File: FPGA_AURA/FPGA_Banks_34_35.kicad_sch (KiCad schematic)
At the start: 15 parts, among them U1 XC7A35T-2FTG256C

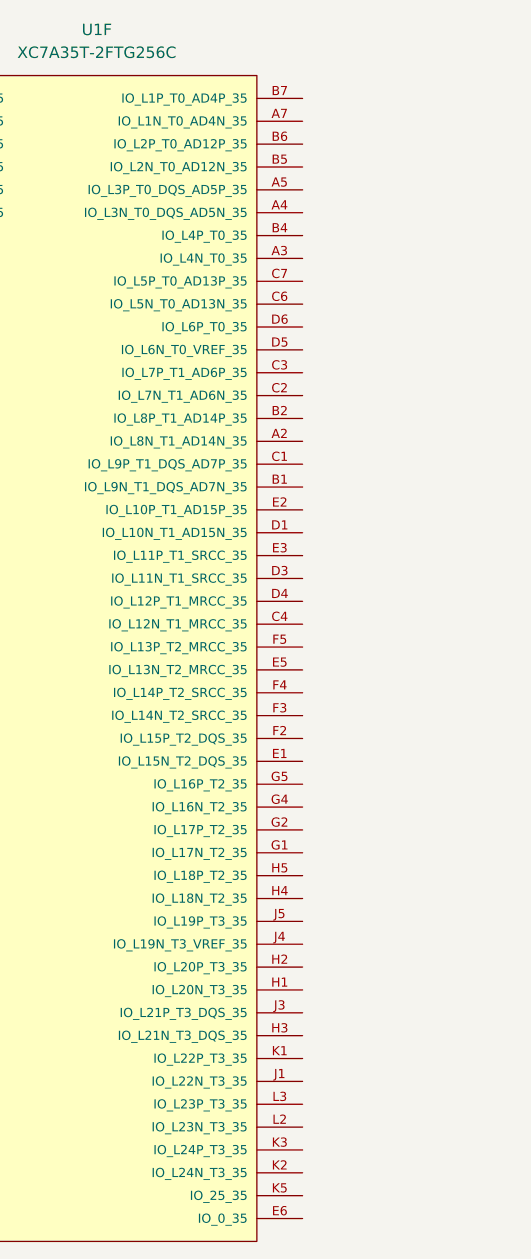
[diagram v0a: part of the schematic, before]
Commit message: Started pinout after successful Vivado bitstream generation.
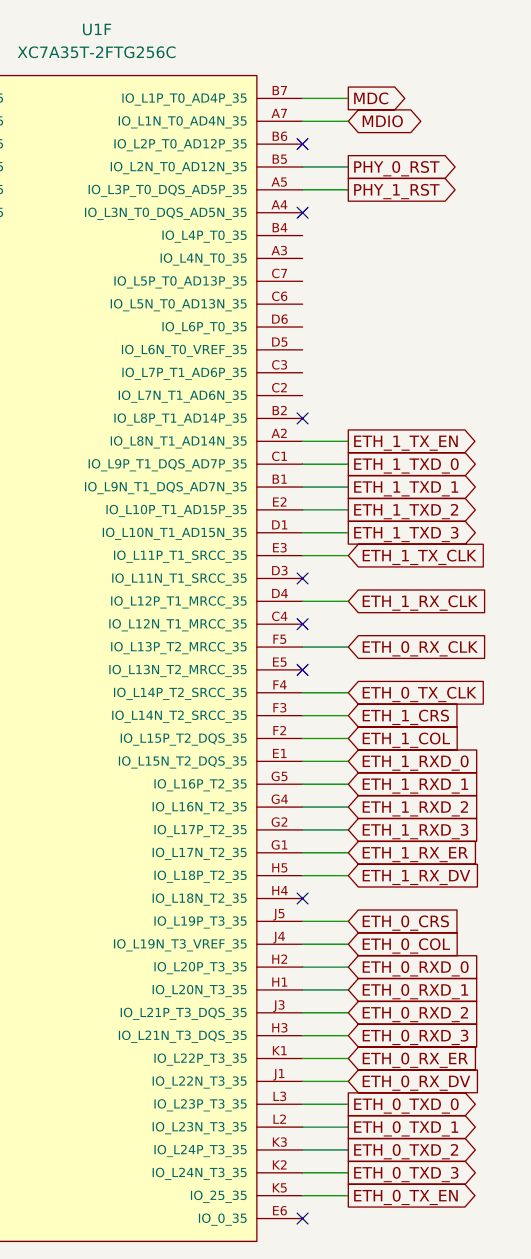
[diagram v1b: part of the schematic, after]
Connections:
- net ETH_1_TX_EN: now reaches U1.A2 (IO_L8N_T1_AD14N_35)
- net PHY_1_RST: now reaches U1.A5 (IO_L3P_T0_DQS_AD5P_35)
- net MDIO: now reaches U1.A7 (IO_L1N_T0_AD4N_35)
- net ETH_1_TXD_1: now reaches U1.B1 (IO_L9N_T1_DQS_AD7N_35)
- net PHY_0_RST: now reaches U1.B5 (IO_L2N_T0_AD12N_35)
- net MDC: now reaches U1.B7 (IO_L1P_T0_AD4P_35)
- net ETH_1_TXD_0: now reaches U1.C1 (IO_L9P_T1_DQS_AD7P_35)
- net ETH_1_TXD_3: now reaches U1.D1 (IO_L10N_T1_AD15N_35)
- net ETH_1_RX_CLK: now reaches U1.D4 (IO_L12P_T1_MRCC_35)
- net ETH_1_RXD_0: now reaches U1.E1 (IO_L15N_T2_DQS_35)
- net ETH_1_TXD_2: now reaches U1.E2 (IO_L10P_T1_AD15P_35)
- net ETH_1_TX_CLK: now reaches U1.E3 (IO_L11P_T1_SRCC_35)
- net ETH_1_COL: now reaches U1.F2 (IO_L15P_T2_DQS_35)
- net ETH_1_CRS: now reaches U1.F3 (IO_L14N_T2_SRCC_35)
- net ETH_0_TX_CLK: now reaches U1.F4 (IO_L14P_T2_SRCC_35)
- net ETH_0_RX_CLK: now reaches U1.F5 (IO_L13P_T2_MRCC_35)
- net ETH_1_RX_ER: now reaches U1.G1 (IO_L17N_T2_35)
- net ETH_1_RXD_3: now reaches U1.G2 (IO_L17P_T2_35)
- net ETH_1_RXD_2: now reaches U1.G4 (IO_L16N_T2_35)
- net ETH_1_RXD_1: now reaches U1.G5 (IO_L16P_T2_35)
- net ETH_0_RXD_1: now reaches U1.H1 (IO_L20N_T3_35)
- net ETH_0_RXD_0: now reaches U1.H2 (IO_L20P_T3_35)
- net ETH_0_RXD_3: now reaches U1.H3 (IO_L21N_T3_DQS_35)
- net ETH_1_RX_DV: now reaches U1.H5 (IO_L18P_T2_35)
- net ETH_0_RX_DV: now reaches U1.J1 (IO_L22N_T3_35)
- net ETH_0_RXD_2: now reaches U1.J3 (IO_L21P_T3_DQS_35)
- net ETH_0_COL: now reaches U1.J4 (IO_L19N_T3_VREF_35)
- net ETH_0_CRS: now reaches U1.J5 (IO_L19P_T3_35)
- net ETH_0_RX_ER: now reaches U1.K1 (IO_L22P_T3_35)
- net ETH_0_TXD_3: now reaches U1.K2 (IO_L24N_T3_35)
- net ETH_0_TXD_2: now reaches U1.K3 (IO_L24P_T3_35)
- net ETH_0_TX_EN: now reaches U1.K5 (IO_25_35)
- net ETH_0_TXD_1: now reaches U1.L2 (IO_L23N_T3_35)
- net ETH_0_TXD_0: now reaches U1.L3 (IO_L23P_T3_35)
- no-connect marks 0 -> 8

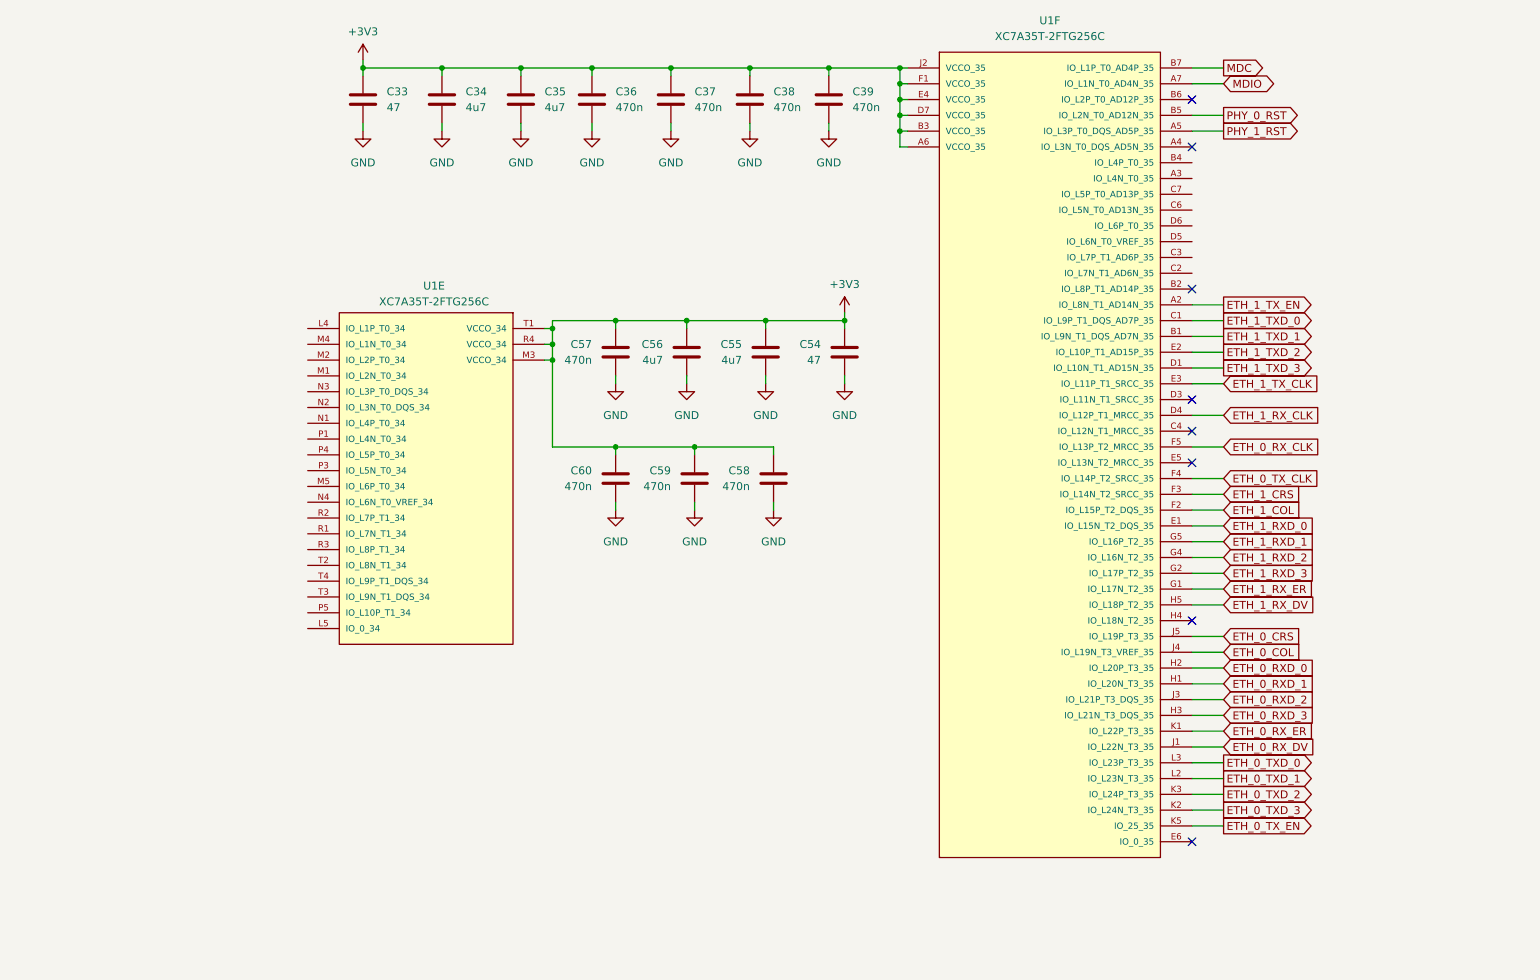
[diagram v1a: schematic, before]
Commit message: Connector pinnout defined loosly. Next is schematic clean-up followed by routing.
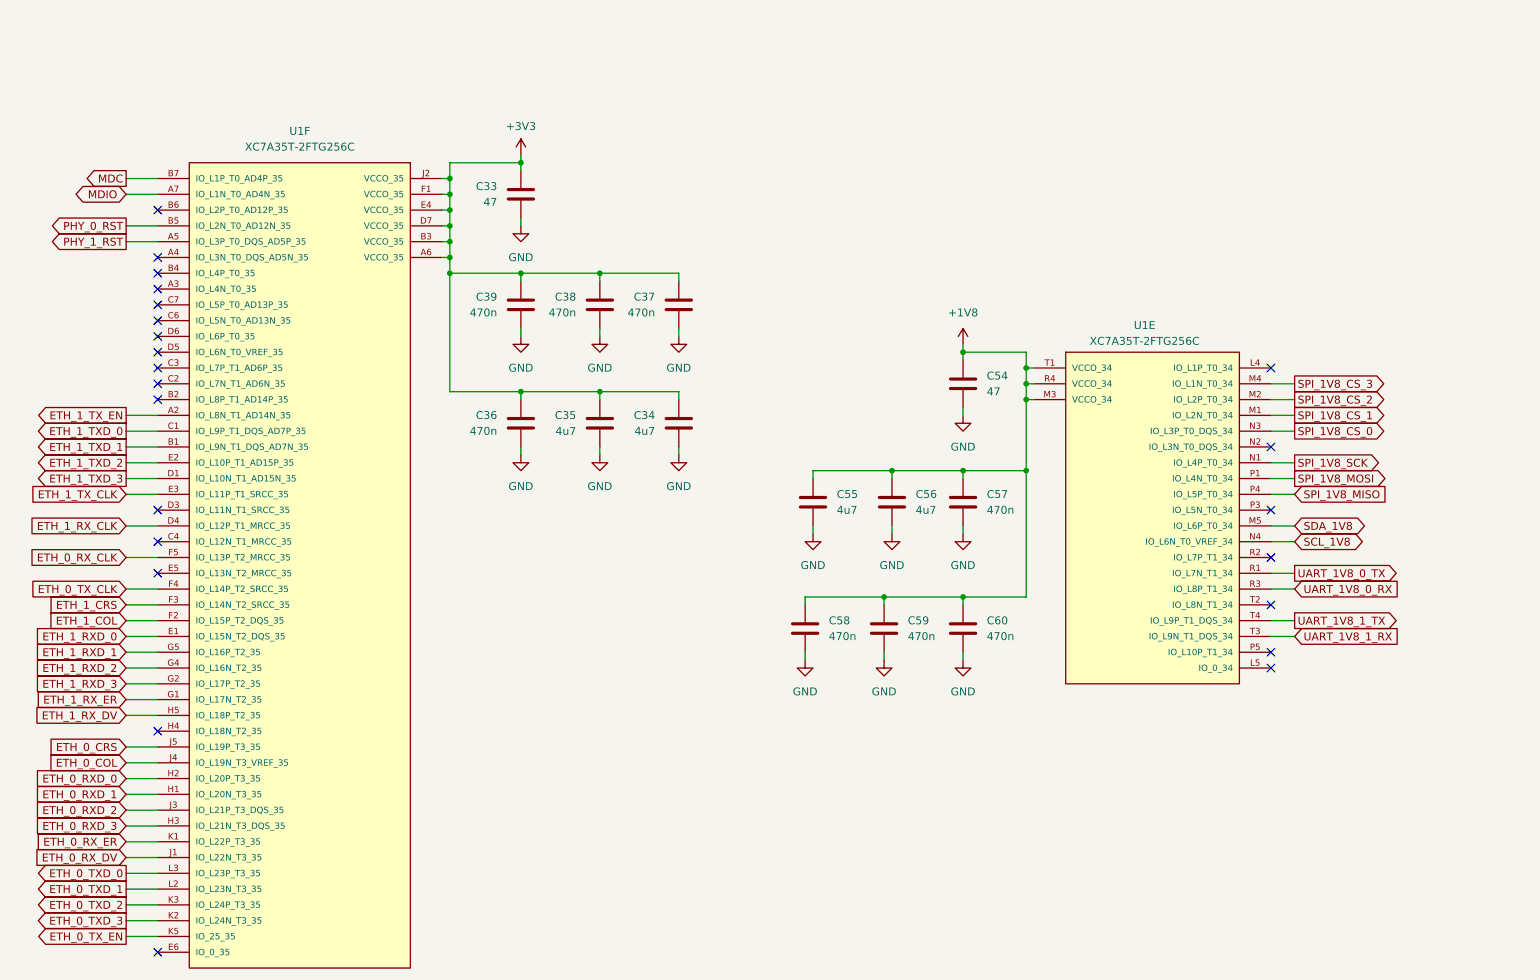
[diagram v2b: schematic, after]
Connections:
- net +3V3: no longer C54.1, C55.1, C56.1, C57.1, C58.1, C59.1, C60.1, U1.M3 (VCCO_34), U1.R4 (VCCO_34), U1.T1 (VCCO_34)
- net SPI_1V8_CS_1: now reaches U1.M1 (IO_L2N_T0_34)
- net SPI_1V8_CS_2: now reaches U1.M2 (IO_L2P_T0_34)
- net SPI_1V8_CS_3: now reaches U1.M4 (IO_L1N_T0_34)
- net SDA_1V8: now reaches U1.M5 (IO_L6P_T0_34)
- net SPI_1V8_SCK: now reaches U1.N1 (IO_L4P_T0_34)
- net SPI_1V8_CS_0: now reaches U1.N3 (IO_L3P_T0_DQS_34)
- net SCL_1V8: now reaches U1.N4 (IO_L6N_T0_VREF_34)
- net SPI_1V8_MOSI: now reaches U1.P1 (IO_L4N_T0_34)
- net SPI_1V8_MISO: now reaches U1.P4 (IO_L5P_T0_34)
- net UART_1V8_0_TX: now reaches U1.R1 (IO_L7N_T1_34)
- net UART_1V8_0_RX: now reaches U1.R3 (IO_L8P_T1_34)
- net UART_1V8_1_RX: now reaches U1.T3 (IO_L9N_T1_DQS_34)
- net UART_1V8_1_TX: now reaches U1.T4 (IO_L9P_T1_DQS_34)
- new net +1V8: C54.1, C55.1, C56.1, C57.1, C58.1, C59.1, C60.1, U1.M3 (VCCO_34), U1.R4 (VCCO_34), U1.T1 (VCCO_34)
- no-connect marks 8 -> 23
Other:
- moved on the sheet: C33, C34, C35, C36, C37, C38, C39, C54, C55, C56, C57, C58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

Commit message: Finished schematic to start routing again, and started MII fanout from connector.
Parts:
- C600: renamed from C33; value 47 -> 47u
- C607: renamed from C54; value 47 -> 47u
- renumbered C39 to C601, C38 to C602, C37 to C603, C36 to C604, C35 to C605, C34 to C606, C57 to C608, C56 to C609, C55 to C610, C60 to C611, C59 to C612, C58 to C613
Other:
- company: (none) -> Alexander Armitage
- title: (none) -> XC7A35T Banks 34, 35
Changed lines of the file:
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@@
 	(generator_version "10.0")
 	(paper "A4")
+	(title_block
+		(title "XC7A35T Banks 34, 35")
+		(company "Alexander Armitage")
+	)
 	(junction
 		(at 196.85 85.09)
@@
 		(dnp no)
 		(fields_autoplaced yes)
-		(property "Reference" "C39"
+		(property "Reference" "C601"
 			(at 111.76 68.5799 0)
 			(show_name no)
@@
 			(project "FPGA_AURA"
 				(path "/3d83cb23-9528-4d06-8969-599520e9eb23/2d3446c8-405c-4eaf-9ac6-0e0b69b3b124"
-					(reference "C39")
+					(reference "C601")
 					(unit 1)
 				)
@@
 		(dnp no)
 		(fields_autoplaced yes)
-		(property "Reference" "C58"
+		(property "Reference" "C613"
 			(at 165.1 120.6499 0)
 			(show_name no)
@@
 			(project "FPGA_AURA"
 				(path "/3d83cb23-9528-4d06-8969-599520e9eb23/2d3446c8-405c-4eaf-9ac6-0e0b69b3b124"
-					(reference "C58")
+					(reference "C613")
 					(unit 1)
 				)
@@
 		(lib_id "Device:C")
 		(at 115.57 88.9 0)
-		(mirror y)
 		(unit 1)
 		(body_style 1)
@@
 		(in_pos_files yes)
 		(dnp no)
-		(fields_autoplaced yes)
-		(property "Reference" "C36"
+		(property "Reference" "C604"
 			(at 111.76 87.6299 0)
 			(show_name no)
@@
 					(size 1.27 1.27)
 				)
-				(justify left)
+				(justify right)
 			)
 		)
@@
 					(size 1.27 1.27)
 				)
-				(justify left)
+				(justify right)
 			)
 		)
 		(property "Footprint" "Capacitor_SMD:C_0402_1005Metric"
-			(at 114.6048 92.71 0)
+			(at 116.5352 92.71 0)
 			(hide yes)
 			(show_name no)
@@
 			(project "FPGA_AURA"
 				(path "/3d83cb23-9528-4d06-8969-599520e9eb23/2d3446c8-405c-4eaf-9ac6-0e0b69b3b124"
-					(reference "C36")
+					(reference "C604")
 					(unit 1)
 				)
@@
 		(lib_id "Device:C")
 		(at 140.97 69.85 0)
-		(mirror y)
 		(unit 1)
 		(body_style 1)
@@
 		(in_pos_files yes)
 		(dnp no)
-		(fields_autoplaced yes)
-		(property "Reference" "C37"
+		(property "Reference" "C603"
 			(at 137.16 68.5799 0)
 			(show_name no)
@@
 					(size 1.27 1.27)
 				)
-				(justify left)
+				(justify right)
 			)
 		)
@@
 					(size 1.27 1.27)
 				)
-				(justify left)
+				(justify right)
 			)
 		)
 		(property "Footprint" "Capacitor_SMD:C_0402_1005Metric"
-			(at 140.0048 73.66 0)
+			(at 141.9352 73.66 0)
 			(hide yes)
 			(show_name no)
@@
 			(project "FPGA_AURA"
 				(path "/3d83cb23-9528-4d06-8969-599520e9eb23/2d3446c8-405c-4eaf-9ac6-0e0b69b3b124"
-					(reference "C37")
+					(reference "C603")
 					(unit 1)
 				)
@@
 		(lib_id "Device:C")
 		(at 140.97 88.9 0)
-		(mirror y)
 		(unit 1)
 		(body_style 1)
@@
 		(in_pos_files yes)
 		(dnp no)
-		(fields_autoplaced yes)
-		(property "Reference" "C34"
+		(property "Reference" "C606"
 			(at 137.16 87.6299 0)
 			(show_name no)
@@
 					(size 1.27 1.27)
 				)
-				(justify left)
+				(justify right)
 			)
 		)
@@
 					(size 1.27 1.27)
 				)
-				(justify left)
+				(justify right)
 			)
 		)
 		(property "Footprint" "Capacitor_SMD:C_0603_1608Metric"
-			(at 140.0048 92.71 0)
+			(at 141.9352 92.71 0)
 			(hide yes)
 			(show_name no)
@@
 			(project "FPGA_AURA"
 				(path "/3d83cb23-9528-4d06-8969-599520e9eb23/2d3446c8-405c-4eaf-9ac6-0e0b69b3b124"
-					(reference "C34")
+					(reference "C606")
 					(unit 1)
 				)
@@
 		(lib_id "Device:C")
 		(at 128.27 88.9 0)
-		(mirror y)
 		(unit 1)
 		(body_style 1)
@@
 		(in_pos_files yes)
 		(dnp no)
-		(fields_autoplaced yes)
-		(property "Reference" "C35"
+		(property "Reference" "C605"
 			(at 124.46 87.6299 0)
 			(show_name no)
@@
 					(size 1.27 1.27)
 				)
-				(justify left)
+				(justify right)
 			)
 		)
@@
 					(size 1.27 1.27)
 				)
-				(justify left)
+				(justify right)
 			)
 		)
 		(property "Footprint" "Capacitor_SMD:C_0603_1608Metric"
-			(at 127.3048 92.71 0)
+			(at 129.2352 92.71 0)
 			(hide yes)
 			(show_name no)
@@
 			(project "FPGA_AURA"
 				(path "/3d83cb23-9528-4d06-8969-599520e9eb23/2d3446c8-405c-4eaf-9ac6-0e0b69b3b124"
-					(reference "C35")
+					(reference "C605")
 					(unit 1)
 				)
@@
 		(lib_id "Device:C")
 		(at 115.57 52.07 0)
-		(mirror y)
 		(unit 1)
 		(body_style 1)
@@
 		(in_pos_files yes)
 		(dnp no)
-		(fields_autoplaced yes)
-		(property "Reference" "C33"
+		(property "Reference" "C600"
 			(at 111.76 50.7999 0)
 			(show_name no)
@@
 					(size 1.27 1.27)
 				)
-				(justify left)
+				(justify right)
 			)
 		)
-		(property "Value" "47"
+		(property "Value" "47u"
 			(at 111.76 53.3399 0)
 			(show_name no)
@@
 					(size 1.27 1.27)
 				)
-				(justify left)
+				(justify right)
 			)
 		)
 		(property "Footprint" "Capacitor_SMD:C_0603_1608Metric"
-			(at 114.6048 55.88 0)
+			(at 116.5352 55.88 0)
 			(hide yes)
 			(show_name no)
@@
 			(project "FPGA_AURA"
 				(path "/3d83cb23-9528-4d06-8969-599520e9eb23/2d3446c8-405c-4eaf-9ac6-0e0b69b3b124"
-					(reference "C33")
+					(reference "C600")
 					(unit 1)
 				)
@@
 		(dnp no)
 		(fields_autoplaced yes)
-		(property "Reference" "C60"
+		(property "Reference" "C611"
 			(at 190.5 120.6499 0)
 			(show_name no)
@@
 			(project "FPGA_AURA"
 				(path "/3d83cb23-9528-4d06-8969-599520e9eb23/2d3446c8-405c-4eaf-9ac6-0e0b69b3b124"
-					(reference "C60")
+					(reference "C611")
 					(unit 1)
 				)
@@
 		(dnp no)
 		(fields_autoplaced yes)
-		(property "Reference" "C55"
+		(property "Reference" "C610"
 			(at 166.37 100.3299 0)
 			(show_name no)
@@
 			(project "FPGA_AURA"
 				(path "/3d83cb23-9528-4d06-8969-599520e9eb23/2d3446c8-405c-4eaf-9ac6-0e0b69b3b124"
-					(reference "C55")
+					(reference "C610")
 					(unit 1)
 				)
@@
 		(dnp no)
 		(fields_autoplaced yes)
-		(property "Reference" "C57"
+		(property "Reference" "C608"
 			(at 190.5 100.3299 0)
 			(show_name no)
@@
 			(project "FPGA_AURA"
 				(path "/3d83cb23-9528-4d06-8969-599520e9eb23/2d3446c8-405c-4eaf-9ac6-0e0b69b3b124"
-					(reference "C57")
+					(reference "C608")
 					(unit 1)
 				)
@@
 		(dnp no)
 		(fields_autoplaced yes)
-		(property "Reference" "C56"
+		(property "Reference" "C609"
 			(at 179.07 100.3299 0)
 			(show_name no)
@@
 			(project "FPGA_AURA"
 				(path "/3d83cb23-9528-4d06-8969-599520e9eb23/2d3446c8-405c-4eaf-9ac6-0e0b69b3b124"
-					(reference "C56")
+					(reference "C609")
 					(unit 1)
 				)
@@
 		(dnp no)
 		(fields_autoplaced yes)
-		(property "Reference" "C59"
+		(property "Reference" "C612"
 			(at 177.8 120.6499 0)
 			(show_name no)
@@
 			(project "FPGA_AURA"
 				(path "/3d83cb23-9528-4d06-8969-599520e9eb23/2d3446c8-405c-4eaf-9ac6-0e0b69b3b124"
-					(reference "C59")
+					(reference "C612")
 					(unit 1)
 				)
@@
 		(dnp no)
 		(fields_autoplaced yes)
-		(property "Reference" "C54"
+		(property "Reference" "C607"
 			(at 190.5 81.2799 0)
 			(show_name no)
@@
 			)
 		)
-		(property "Value" "47"
+		(property "Value" "47u"
 			(at 190.5 83.8199 0)
 			(show_name no)
@@
 			(project "FPGA_AURA"
 				(path "/3d83cb23-9528-4d06-8969-599520e9eb23/2d3446c8-405c-4eaf-9ac6-0e0b69b3b124"
-					(reference "C54")
+					(reference "C607")
 					(unit 1)
 				)
@@
 		(lib_id "Device:C")
 		(at 128.27 69.85 0)
-		(mirror y)
 		(unit 1)
 		(body_style 1)
@@
 		(in_pos_files yes)
 		(dnp no)
-		(fields_autoplaced yes)
-		(property "Reference" "C38"
+		(property "Reference" "C602"
 			(at 124.46 68.5799 0)
 			(show_name no)
@@
 					(size 1.27 1.27)
 				)
-				(justify left)
+				(justify right)
 			)
 		)
@@
 					(size 1.27 1.27)
 				)
-				(justify left)
+				(justify right)
 			)
 		)
 		(property "Footprint" "Capacitor_SMD:C_0402_1005Metric"
-			(at 127.3048 73.66 0)
+			(at 129.2352 73.66 0)
 			(hide yes)
 			(show_name no)
@@
 			(project "FPGA_AURA"
 				(path "/3d83cb23-9528-4d06-8969-599520e9eb23/2d3446c8-405c-4eaf-9ac6-0e0b69b3b124"
-					(reference "C38")
+					(reference "C602")
 					(unit 1)
 				)
